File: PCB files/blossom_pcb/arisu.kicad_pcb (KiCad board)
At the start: 2 copper layers, 369.9 x 155.6 mm, 205 parts, among them J1 Conn_01x02, SW1 SW_Push, SW10 SW_Push, SW11 SW_Push, SW12 SW_Push, SW13 SW_Push, SW14 SW_Push, SW15 SW_Push, SW16 SW_Push, SW17 SW_Push, SW18 SW_Push, SW19 SW_Push, SW2 SW_Push, SW20 SW_Push, SW21 SW_Push, SW22 SW_Push, SW23 SW_Push, SW24 SW_Push, SW25 SW_Push, SW26 SW_Push, SW27 SW_Push, SW28 SW_Push, SW29 SW_Push, SW3 SW_Push, SW30 SW_Push, SW31 SW_Push, SW32 SW_Push, SW33 SW_Push, SW34 SW_Push, SW35 SW_Push, SW36 SW_Push, SW36_Stab1 Stabilizer_Cherry_MX_2.00u, SW37 SW_Push, SW37_Stab1 Stabilizer_Cherry_MX_2.00u, SW38 SW_Push, SW39 SW_Push, SW4 SW_Push, SW40 SW_Push, SW41 SW_Push, SW42 SW_Push, SW43 SW_Push, SW44 SW_Push, SW45 SW_Push, SW46 SW_Push, SW47 SW_Push, SW48 SW_Push, SW49 SW_Push, SW5 SW_Push, SW50 SW_Push, SW51 SW_Push, SW51_Stab1 Stabilizer_Cherry_MX_2.00u, SW52 SW_Push, SW53 SW_Push, SW54 SW_Push, SW54_Stab1 Stabilizer_Cherry_MX_2.00u, SW55 SW_Push, SW56 SW_Push, SW57 SW_Push, SW58 SW_Push, SW59 SW_Push, SW6 SW_Push, SW60 SW_Push, SW61 SW_Push, SW62 SW_Push, SW63 SW_Push, SW64 SW_Push, SW65 SW_Push, SW66 SW_Push, SW67 SW_Push, SW68 SW_Push, SW69 SW_Push, SW7 SW_Push, SW70 SW_Push, SW71 SW_Push, SW72 SW_Push, SW73 SW_Push, SW74 SW_Push, SW75 SW_Push, SW76 SW_Push, SW8 SW_Push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

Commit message: Better traces.
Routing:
- net /GPIO18: track 94.6 -> 250.2 mm
- net /GPIO8: track 424.0 -> 567.1 mm, vias 2 -> 6
- net /GPIO11: track 204.3 -> 339.9 mm, vias 6 -> 7
- net /GPIO19: track 95.8 -> 228.8 mm
- net /GPIO20: track 103.1 -> 210.2 mm
- net /GPIO17: track 146.0 -> 250.8 mm
- net /GPIO13: track 89.6 -> 186.9 mm, vias 6 -> 7
- net /GPIO12: track 157.5 -> 243.2 mm
- net /GPIO24: track 187.5 -> 271.6 mm
- net /GPIO16: track 135.6 -> 214.3 mm
- net /GPIO25: track 214.3 -> 292.5 mm
- net /GPIO21: track 125.7 -> 202.4 mm, vias 2 -> 6
- net /GPIO23: track 165.7 -> 241.9 mm
- net /GPIO22: track 145.7 -> 221.9 mm
- net /GPIO15: track 57.5 -> 122.2 mm, vias 3 -> 1
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- removed copper zone on F.Cu, net /GPIO12
- removed copper zone on F.Cu, net /GPIO13
- removed copper zone on F.Cu, net /GPIO21
- removed copper zone on F.Cu, net /GPIO22
- removed copper zone on F.Cu, net /GPIO23
- removed copper zone on F.Cu, net /GPIO24
- removed copper zone on F.Cu, net /GPIO25

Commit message: probably final without usb
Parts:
- removed the H1 at (-76.7, -0.69)
- removed the H2 at (-76.7, 6.26)
- removed the H3 at (-76.7, 13.2)
- removed the H4 at (-76.7, 20.2)
- removed the H5 at (-70.2, -1.19)
- removed the H6 at (-70.2, 4.76)
- removed SW36_Stab1, SW37_Stab1, SW51_Stab1, SW54_Stab1: Stabilizer_Cherry_MX_2.00u, PCM_Mounting_Keyboard_Stabilizer:Stabilizer_Cherry_MX_2.00u
- R4: moved to B.Cu
- moved H3 453.6 mm to (376.4, 128.1)
- moved H5 429.6 mm to (376.4, 23.6)
- moved H2 307.8 mm to (194.4, 171.6)
- moved H1 259.9 mm to (194.4, 23.6)
- moved H4 142.9 mm to (13.9, 128.1)
- moved H6 68.8 mm to (13.9, 23.1)
- moved C7 34.5 mm to (190.6, 48.5)
- moved C8 34.5 mm to (190.6, 52.7)
- moved C6 34.5 mm to (190.6, 44.8)
- moved C17 17.5 mm to (196.6, 41.6)
- moved C3 17.5 mm to (212.5, 45.9)
- moved C5 17.5 mm to (196.6, 44.8)
- moved U1 17.5 mm to (205.4, 43.5)
- moved C1 9.33 mm to (194.2, 91.4)
- moved Y1 9.33 mm to (194.2, 81.1)
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- renumbered H7 to H1, H8 to H2, H9 to H3, H10 to H4, H11 to H5, H12 to H6
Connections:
- D1 pad 1: /GPIO5 -> /row0
- D10 pad 1: /GPIO5 -> /row0
- D11 pad 1: /GPIO5 -> /row0
- D12 pad 1: /GPIO5 -> /row0
- D13 pad 1: /GPIO5 -> /row0
- D14 pad 1: /GPIO5 -> /row0
- D15 pad 1: /GPIO6 -> /row1
- D16 pad 1: /GPIO6 -> /row1
- D17 pad 1: /GPIO6 -> /row1
- D18 pad 1: /GPIO6 -> /row1
- D19 pad 1: /GPIO6 -> /row1
- D2 pad 1: /GPIO5 -> /row0
- D20 pad 1: /GPIO6 -> /row1
- D21 pad 1: /GPIO6 -> /row1
- D22 pad 1: /GPIO6 -> /row1
- D23 pad 1: /GPIO6 -> /row1
- D24 pad 1: /GPIO6 -> /row1
- D25 pad 1: /GPIO6 -> /row1
- D26 pad 1: /GPIO6 -> /row1
- D27 pad 1: /GPIO6 -> /row1
- D28 pad 1: /GPIO6 -> /row1
- D29 pad 1: /GPIO7 -> /row2
- D3 pad 1: /GPIO5 -> /row0
- D30 pad 1: /GPIO7 -> /row2
- D31 pad 1: /GPIO7 -> /row2
- D32 pad 1: /GPIO7 -> /row2
- D33 pad 1: /GPIO7 -> /row2
- D34 pad 1: /GPIO7 -> /row2
- D35 pad 1: /GPIO7 -> /row2
- D36 pad 1: /GPIO7 -> /row2
- D37 pad 1: /GPIO7 -> /row2
- D38 pad 1: /GPIO7 -> /row2
- D39 pad 1: /GPIO7 -> /row2
- D4 pad 1: /GPIO5 -> /row0
- D40 pad 1: /GPIO7 -> /row2
- D41 pad 1: /GPIO7 -> /row2
- D42 pad 1: /GPIO7 -> /row2
- D43 pad 1: /GPIO7 -> /row2
- D44 pad 1: /GPIO7 -> /row2
- D45 pad 1: /GPIO8 -> /row3
- D46 pad 1: /GPIO8 -> /row3
- D47 pad 1: /GPIO8 -> /row3
- D48 pad 1: /GPIO8 -> /row3
- D49 pad 1: /GPIO8 -> /row3
- D5 pad 1: /GPIO5 -> /row0
- D50 pad 1: /GPIO8 -> /row3
- D51 pad 1: /GPIO8 -> /row3
- D52 pad 1: /GPIO8 -> /row3
- D53 pad 1: /GPIO8 -> /row3
- D54 pad 1: /GPIO8 -> /row3
- D55 pad 1: /GPIO8 -> /row3
- D56 pad 1: /GPIO8 -> /row3
- D57 pad 1: /GPIO8 -> /row3
- D58 pad 1: /GPIO8 -> /row3
- D59 pad 1: /GPIO8 -> /row3
- D6 pad 1: /GPIO5 -> /row0
- D60 pad 1: /GPIO8 -> /row3
- D61 pad 1: /GPIO9 -> /row4
- D62 pad 1: /GPIO9 -> /row4
- D63 pad 1: /GPIO9 -> /row4
- D64 pad 1: /GPIO9 -> /row4
- D65 pad 1: /GPIO9 -> /row4
- D66 pad 1: /GPIO9 -> /row4
- D67 pad 1: /GPIO9 -> /row4
- D68 pad 1: /GPIO9 -> /row4
- D69 pad 1: /GPIO9 -> /row4
- D7 pad 1: /GPIO5 -> /row0
- D70 pad 1: /GPIO9 -> /row4
- D71 pad 1: /GPIO9 -> /row4
- D72 pad 1: /GPIO9 -> /row4
- D73 pad 1: /GPIO9 -> /row4
- D74 pad 1: /GPIO9 -> /row4
- D75 pad 1: /GPIO9 -> /row4
- D76 pad 1: /GPIO9 -> /row4
- D8 pad 1: /GPIO5 -> /row0
- D9 pad 1: /GPIO5 -> /row0
- R101 pad 1: /GPIO4 -> /PWM
- SW1 pad 1: /GPIO10 -> /col0
- SW10 pad 1: /GPIO21 -> /col11
- SW11 pad 1: /GPIO22 -> /col12
- SW12 pad 1: /GPIO23 -> /col13
- SW13 pad 1: /GPIO24 -> /col14
- SW14 pad 1: /GPIO25 -> /col15
- SW15 pad 1: /GPIO10 -> /col0
- SW16 pad 1: /GPIO11 -> /col1
- SW17 pad 1: /GPIO18 -> /col2
- SW18 pad 1: /GPIO19 -> /col3
- SW19 pad 1: /GPIO20 -> /col4
- SW2 pad 1: /GPIO11 -> /col1
- SW20 pad 1: /GPIO17 -> /col5
- SW21 pad 1: /GPIO16 -> /col6
- SW22 pad 1: /GPIO13 -> /col9
- SW23 pad 1: /GPIO12 -> /col10
- SW24 pad 1: /GPIO21 -> /col11
- SW25 pad 1: /GPIO22 -> /col12
- SW26 pad 1: /GPIO23 -> /col13
- SW27 pad 1: /GPIO24 -> /col14
- SW28 pad 1: /GPIO25 -> /col15
- SW29 pad 1: /GPIO10 -> /col0
- SW3 pad 1: /GPIO18 -> /col2
- SW30 pad 1: /GPIO11 -> /col1
- SW31 pad 1: /GPIO18 -> /col2
- SW32 pad 1: /GPIO19 -> /col3
- SW33 pad 1: /GPIO20 -> /col4
- SW34 pad 1: /GPIO17 -> /col5
- SW35 pad 1: /GPIO16 -> /col6
- SW36 pad 1: /GPIO15 -> /col7
- SW37 pad 1: /GPIO14 -> /col8
- SW38 pad 1: /GPIO13 -> /col9
- SW39 pad 1: /GPIO12 -> /col10
- SW4 pad 1: /GPIO19 -> /col3
- SW40 pad 1: /GPIO21 -> /col11
- SW41 pad 1: /GPIO22 -> /col12
- SW42 pad 1: /GPIO23 -> /col13
- SW43 pad 1: /GPIO24 -> /col14
- SW44 pad 1: /GPIO25 -> /col15
- SW45 pad 1: /GPIO10 -> /col0
- SW46 pad 1: /GPIO11 -> /col1
- SW47 pad 1: /GPIO18 -> /col2
- SW48 pad 1: /GPIO19 -> /col3
- SW49 pad 1: /GPIO20 -> /col4
- SW5 pad 1: /GPIO20 -> /col4
- SW50 pad 1: /GPIO17 -> /col5
- SW51 pad 1: /GPIO16 -> /col6
- SW52 pad 1: /GPIO15 -> /col7
- SW53 pad 1: /GPIO14 -> /col8
- SW54 pad 1: /GPIO13 -> /col9
- SW55 pad 1: /GPIO12 -> /col10
- SW56 pad 1: /GPIO21 -> /col11
- SW57 pad 1: /GPIO22 -> /col12
- SW58 pad 1: /GPIO23 -> /col13
- SW59 pad 1: /GPIO24 -> /col14
- SW6 pad 1: /GPIO17 -> /col5
- SW60 pad 1: /GPIO25 -> /col15
- SW61 pad 1: /GPIO10 -> /col0
- SW62 pad 1: /GPIO11 -> /col1
- SW63 pad 1: /GPIO18 -> /col2
- SW64 pad 1: /GPIO19 -> /col3
- SW65 pad 1: /GPIO20 -> /col4
- SW66 pad 1: /GPIO17 -> /col5
- SW67 pad 1: /GPIO16 -> /col6
- SW68 pad 1: /GPIO15 -> /col7
- SW69 pad 1: /GPIO14 -> /col8
- SW7 pad 1: /GPIO16 -> /col6
- SW70 pad 1: /GPIO13 -> /col9
- SW71 pad 1: /GPIO12 -> /col10
- SW72 pad 1: /GPIO21 -> /col11
- SW73 pad 1: /GPIO22 -> /col12
- SW74 pad 1: /GPIO23 -> /col13
- SW75 pad 1: /GPIO24 -> /col14
- SW76 pad 1: /GPIO25 -> /col15
- SW8 pad 1: /GPIO13 -> /col9
- SW9 pad 1: /GPIO12 -> /col10
- U3 pad 14: /GPIO11 -> /row4
- U3 pad 15: /GPIO12 -> /row3
- U3 pad 16: /GPIO13 -> /row2
- U3 pad 17: /GPIO14 -> /row1
- U3 pad 18: /GPIO15 -> /row0
- U3 pad 2: /GPIO0 -> /col15
- U3 pad 27: /GPIO16 -> /col8
- U3 pad 28: /GPIO17 -> /col7
- U3 pad 3: /GPIO1 -> /col14
- U3 pad 35: /GPIO23 -> /col6
- U3 pad 36: /GPIO24 -> /col5
- U3 pad 37: /GPIO25 -> /col4
- U3 pad 38: /GPIO26_ADC0 -> /col3
- U3 pad 39: /GPIO27_ADC1 -> /col2
- U3 pad 4: /GPIO2 -> /col13
- U3 pad 40: /GPIO28_ADC2 -> /col1
- U3 pad 41: /GPIO29_ADC3 -> /col0
- U3 pad 5: /GPIO3 -> /col12
- U3 pad 6: /GPIO4 -> /col11
- U3 pad 7: /GPIO5 -> /col10
- U3 pad 8: /GPIO6 -> /col9
- U3 pad 9: /GPIO7 -> /PWM
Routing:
- net /GPIO8: track 567.1 -> 0.00 mm, vias 6 -> 0
- net /row3: track 0.00 -> 523.2 mm, vias 0 -> 7
- net /GPIO7: track 507.7 -> 0.00 mm, vias 4 -> 0
- net /GPIO9: track 501.5 -> 0.00 mm, vias 4 -> 0
- net /row4: track 0.00 -> 494.9 mm
- net /row2: track 0.00 -> 487.3 mm, vias 0 -> 5
- net /row0: track 0.00 -> 377.4 mm, vias 0 -> 3
- net /GPIO5: track 372.3 -> 0.00 mm, vias 4 -> 0
- net /GPIO6: track 368.2 -> 0.00 mm, vias 3 -> 0
- net /row1: track 0.00 -> 361.8 mm, vias 0 -> 3
- net /GPIO11: track 339.9 -> 0.00 mm, vias 7 -> 0
- net /GPIO10: track 321.5 -> 0.00 mm, vias 8 -> 0
- net /col0: track 0.00 -> 296.8 mm, vias 0 -> 6
- net /GPIO25: track 292.5 -> 0.00 mm, vias 6 -> 0
- net /col15: track 0.00 -> 276.4 mm, vias 0 -> 6
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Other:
- board size 369.9 x 155.6 mm -> 370.5 x 156 mm
- rule solder_mask_min_width: 0.25 -> 0.09

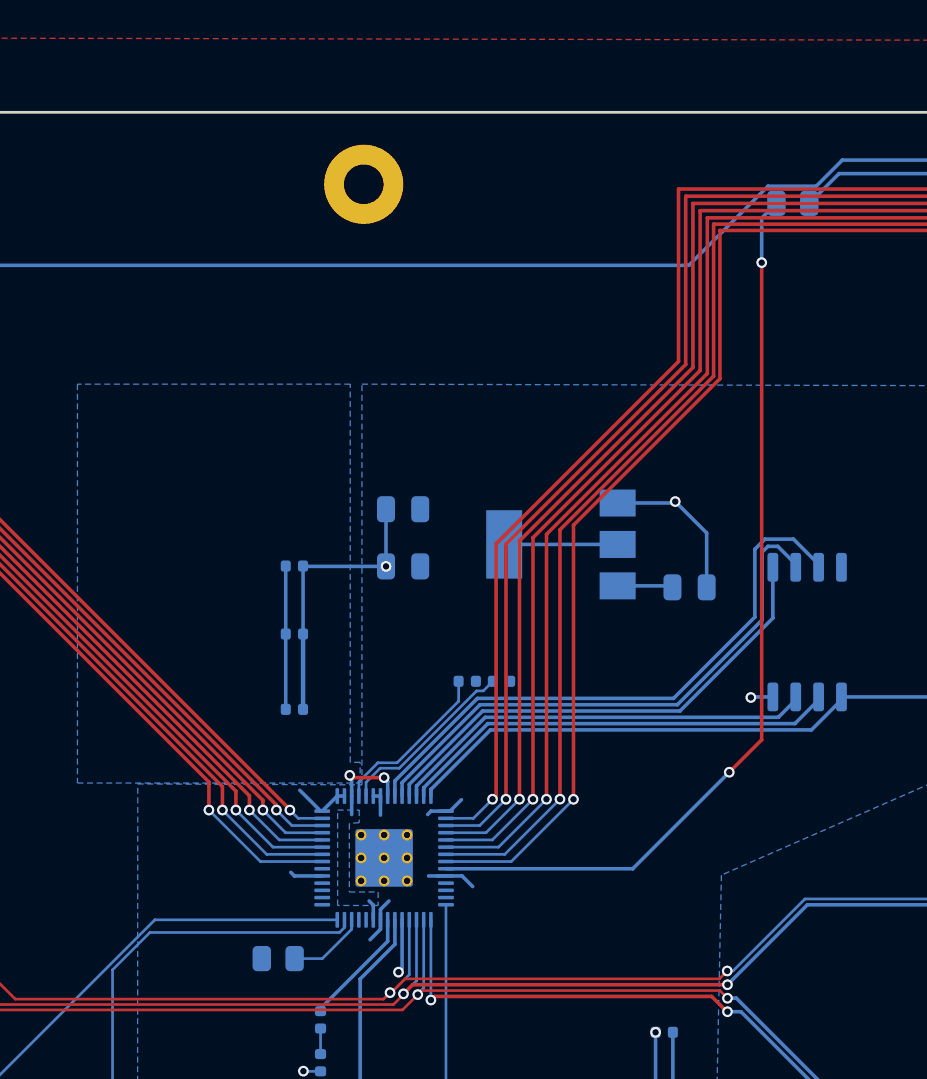
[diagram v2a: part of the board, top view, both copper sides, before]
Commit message: Added usb
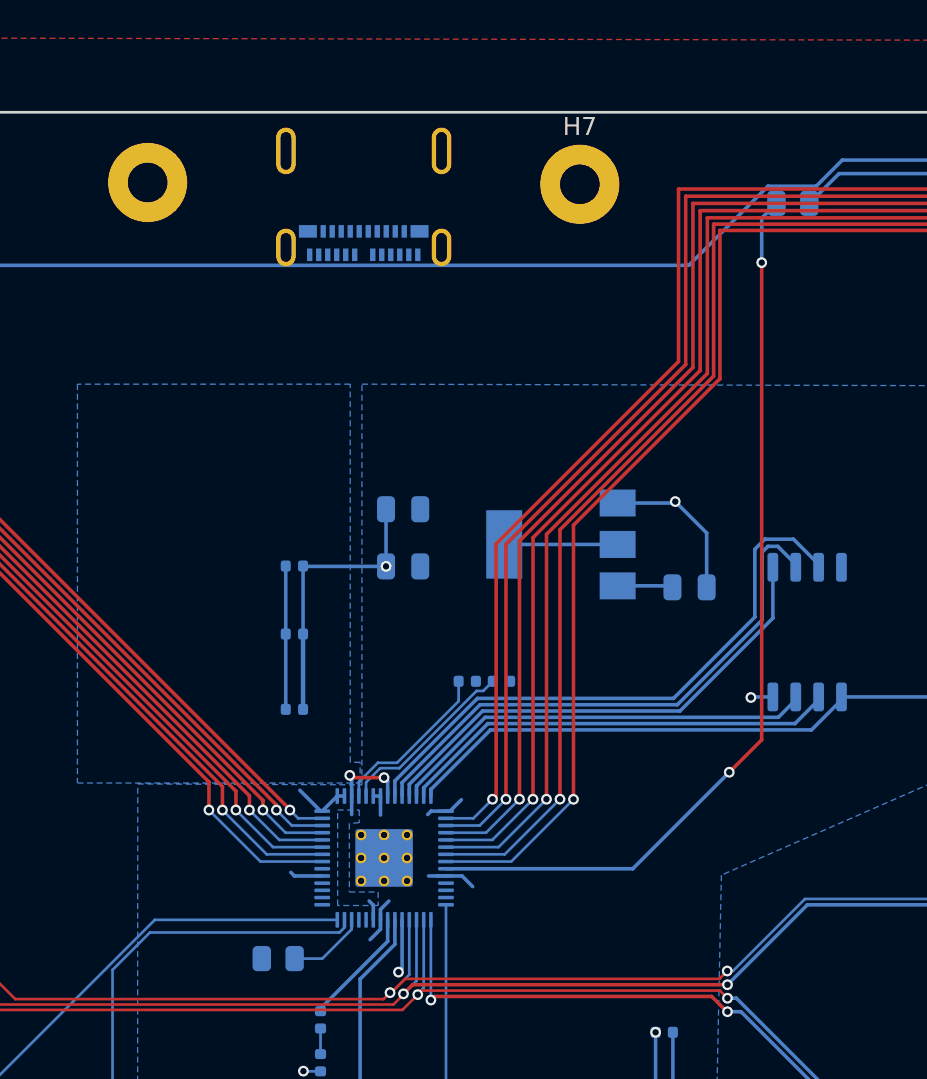
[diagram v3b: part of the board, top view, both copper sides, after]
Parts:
- added H7: MountingHole, MountingHole:MountingHole_2.2mm_M2_Pad, F.Cu at (206.4, 23.6)
- added USB1: USB_C_Receptacle_Molex_105450-0101, Connector_USB:USB_C_Receptacle_Molex_105450-0101, B.Cu at (194.4, 24.2)
- moved H1 12.0 mm to (182.4, 23.4)

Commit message: lots of stuff
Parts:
- removed R2: DNF, Capacitor_SMD:C_0402_1005Metric
- J1: moved to F.Cu
- USB1: value USB_C_Receptacle_Molex_105450-0101 -> USB_C_Plug_USB2.0
- moved J1 2.52 mm to (226.9, 45.2)
- moved R1 2.10 mm to (226.8, 48.4)
- moved R5 1.70 mm to (200.6, 50.5), turned to 0 degrees
- moved R6 1.68 mm to (198.7, 50.5)
- moved USB1 0.13 mm to (194.5, 24.1)
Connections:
- USB1 pad A1: (no net) -> GND
- USB1 pad A12: (no net) -> GND
- USB1 pad A4: (no net) -> VBUS
- USB1 pad A5: (no net) -> unconnected-(USB1-CC-PadA5)
- USB1 pad A6: (no net) -> /USB_D+
- USB1 pad A7: (no net) -> /USB_D-
- USB1 pad A9: (no net) -> VBUS
- USB1 pad B1: (no net) -> GND
- USB1 pad B12: (no net) -> GND
- USB1 pad B4: (no net) -> VBUS
- USB1 pad B5: (no net) -> unconnected-(USB1-VCONN-PadB5)
- USB1 pad B9: (no net) -> VBUS
- USB1 pad S1: (no net) -> GND
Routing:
- net VBUS: track 3.08 -> 33.9 mm
- net /USB_D+: track 0.00 -> 25.6 mm
- net /USB_D-: track 0.00 -> 25.1 mm, vias 0 -> 2
- net +3V3: track 50.7 -> 44.4 mm
- net /QSPI_SS: track 36.0 -> 32.6 mm
- net GND: track 64.1 -> 61.1 mm, vias 15 -> 16
- net VCC: track 681.9 -> 683.5 mm, vias 0 -> 2

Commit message: Cleanup
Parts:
- removed J1: Conn_01x02, Connector_PinHeader_2.54mm:PinHeader_1x02_P2.54mm_Vertical
- added BOOT1: K2-6639DP-B4SW-04, Button_Switch_THT:SW_PUSH_6mm, F.Cu at (226.8, 64.4)
- added P1: Conn_ARM_JTAG_SWD_10, Connector:JLINK_NEEDLE, F.Cu at (175.6, 79.2)
- added R2: 5.1k, Resistor_SMD:R_01005_0402Metric, B.Cu at (193.2, 29.2)
- added R7: 5.1k, Resistor_SMD:R_01005_0402Metric, B.Cu at (193.9, 29.2)
- added R8: 1k, Resistor_SMD:R_01005_0402Metric, B.Cu at (188.4, 28.2)
- added RST1: K2-6639DP-B4SW-04, Button_Switch_THT:SW_PUSH_6mm, F.Cu at (162.4, 71.2)
- Y1: value ABLS-12.000MHZ-B4-T -> X49SM12MSB2SC; footprint RP2040_minimal:Crystal_SMD_HC49-US -> PCM_Crystal_AKL:Crystal_SMD_HC49-SD
- moved C9 39.3 mm to (203.4, 62.3)
- moved C11 33.3 mm to (203.4, 65.2)
- moved C4 29.5 mm to (220.9, 42.8), turned to 90 degrees
- moved C12 28.1 mm to (203.4, 66.6)
- moved C10 27.1 mm to (203.4, 63.7)
- moved C16 24.8 mm to (205.3, 62.3), turned to 0 degrees
- moved C15 19.7 mm to (205.3, 63.8), turned to 0 degrees
- moved C5 16.0 mm to (212.6, 43.5), turned to 0 degrees
- moved C14 14.4 mm to (205.3, 65.2), turned to 0 degrees
- moved R1 10.7 mm to (222.3, 58.0), turned to -90 degrees
- moved C13 9.88 mm to (205.3, 66.7), turned to 0 degrees
- moved C6 9.00 mm to (190.3, 53.8), turned to 45 degrees
- moved R5 7.00 mm to (194.8, 54.5), turned to -90 degrees
- moved R6 6.31 mm to (193.8, 54.5), turned to -90 degrees
- moved C7 5.95 mm to (191.0, 54.5), turned to 45 degrees
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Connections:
- D101 pad 1: VCC -> VBUS
- D102 pad 1: VCC -> VBUS
- D103 pad 1: VCC -> VBUS
- D104 pad 1: VCC -> VBUS
- D105 pad 1: VCC -> VBUS
- D106 pad 1: VCC -> VBUS
- D107 pad 1: VCC -> VBUS
- D108 pad 1: VCC -> VBUS
- R1 pad 2: /~{USB_BOOT} -> Net-(BOOT1-Pad2)
- USB1 pad A5: unconnected-(USB1-CC-PadA5) -> Net-(USB1-CC)
- USB1 pad B5: unconnected-(USB1-VCONN-PadB5) -> Net-(USB1-VCONN)
- USB1 pad S1: GND -> Net-(USB1-SHIELD)
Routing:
- net VBUS: track 33.9 -> 905.0 mm, vias 0 -> 5
- net VCC: track 683.5 -> 0.00 mm, vias 2 -> 0
- net /RUN: track 4.37 -> 49.9 mm, vias 0 -> 2
- net GND: track 61.1 -> 34.7 mm, vias 16 -> 27
- net /row0: track 377.4 -> 402.8 mm
- net SWDIO: track 0.00 -> 25.2 mm, vias 0 -> 1
- net SWCLK: track 0.00 -> 25.2 mm, vias 0 -> 1
- net +3V3: track 44.4 -> 21.8 mm, vias 0 -> 2
- net Net-(USB1-SHIELD): track 0.00 -> 21.2 mm
- net /row1: track 361.8 -> 376.7 mm
- net Net-(BOOT1-Pad2): track 0.00 -> 12.4 mm
- net /col8: track 138.9 -> 146.8 mm
- net +1V1: track 14.7 -> 6.94 mm
- net Net-(U3-USB_DP): track 10.4 -> 2.63 mm
- net Net-(U3-USB_DM): track 9.36 -> 2.68 mm
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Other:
- board text added: "BOOT"
- board text added: "RESET"
